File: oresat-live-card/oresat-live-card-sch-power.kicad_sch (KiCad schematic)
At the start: 116 parts, among them Q2 PMV45EN2R, Q3 DMP2240UDM-7, Q4 PMV45EN2R, Q5 DMP3050LVT-7, Q6 DMP3050LVT-7, U12 MIC842LYC5, U13 MIC842LYC5, U14 MAX4211, U15 LTC3624-5, U16 MAX7310, U21 TLV73311, U22 TS5A21366, U5 LTC3624-5

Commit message: Updated OPD / power page and synced with CFC processor, fixed layout issues.
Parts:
- added TP20, TP21, TP27, TP29: TEST-POINT, oresat-misc:TestPoint_Pad_D1.0mm, symbol oresat-misc:Test-Point-1mm-round
- D6, D7, D8, D9: value GREEN -> GRN
- Q3: value DMP2240UDM-7 -> DMP2240UDM; symbol oresat-transistors:DMP2240UDM-7 -> Transistor_FET:Q_Dual_PMOS_G1S2G2D2S1D1
- R50: value 0 -> 10k; DPN P0.0GCT-ND -> P10.0KHCT-ND; MPN ERJ-3GEY0R00V -> ERJ-3EKF1002V
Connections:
- net GND: now also TP20.1, TP21.1, TP27.1, TP29.1
- net at R51.2, TP57.1, U14.10 (CIN1+): now also R50.2; no longer R50.1
- net at U14.14 (IOUT): now also R50.1; no longer R50.2
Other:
- note added: "MAX7310 Address Selection R54, R55, R57 = 0x1B"
- note removed: "Address selection for Card (See MAX7310 datasheet)"
- note removed: "FIXME"
- note removed: "Install R54, R55, and R57 for Address 0x1B"
- note removed: "OreSat Power Enable (PEN)"
- moved on the sheet: C74, D6, R20, R22, R60, R92, R93, TP24, TP26, TP53, U22

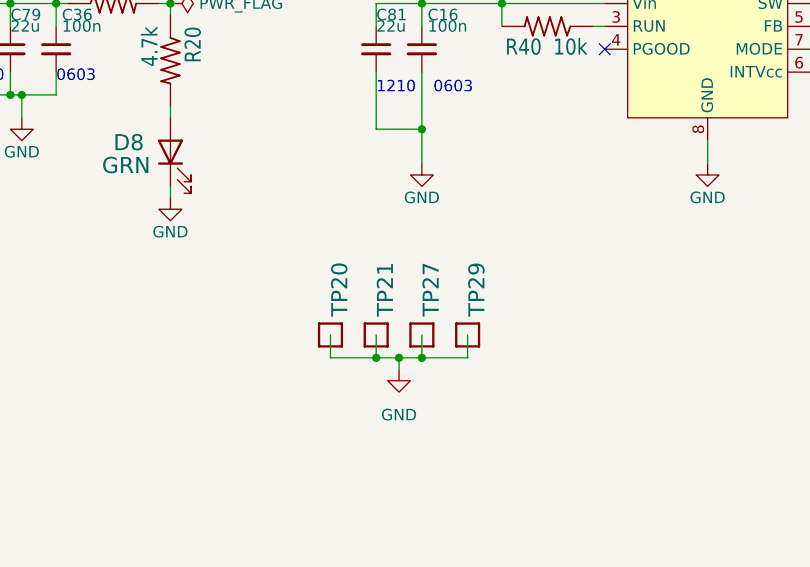
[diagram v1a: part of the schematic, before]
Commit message: Updated SIP A, B, and C. Lots of cleanup of crazy routing - this board is long in the tooth and has been rerouted several times, so there's a lot of crazy routing. Cleaning up a bit is really helping.
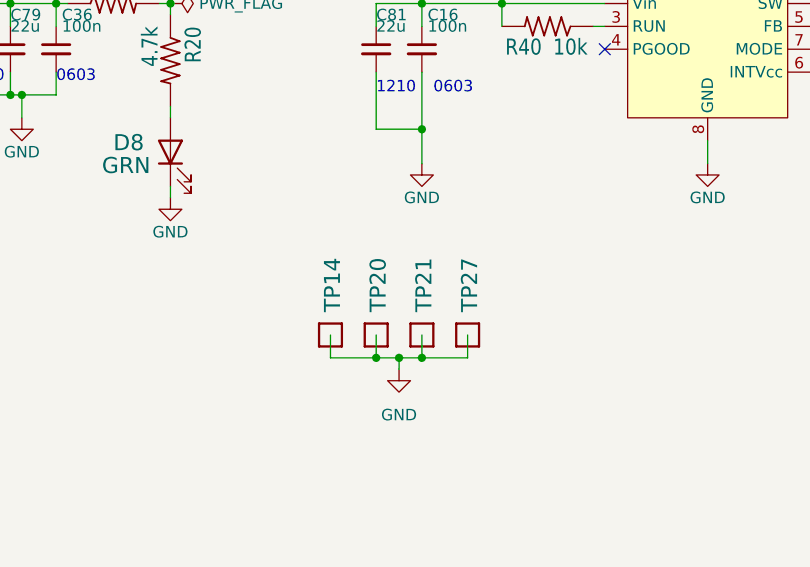
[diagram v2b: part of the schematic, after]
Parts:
- removed TP29: TEST-POINT, oresat-misc:TestPoint_Pad_D1.0mm, symbol oresat-misc:Test-Point-1mm-round
- added TP14: TEST-POINT, oresat-misc:TestPoint-0.75mm-th, symbol oresat-misc:Test-Point-1mm-round
- TP20, TP21, TP27: footprint oresat-misc:TestPoint_Pad_D1.0mm -> oresat-misc:TestPoint-0.75mm-th
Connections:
- net GND: now also TP14.1

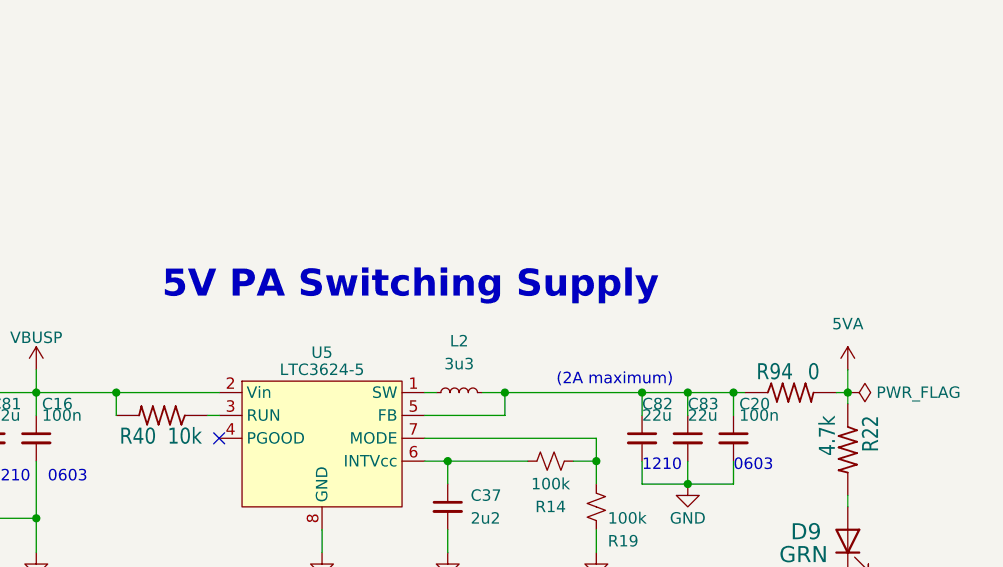
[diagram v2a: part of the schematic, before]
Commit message: Clean up DRC errors, thermistor routing clenup
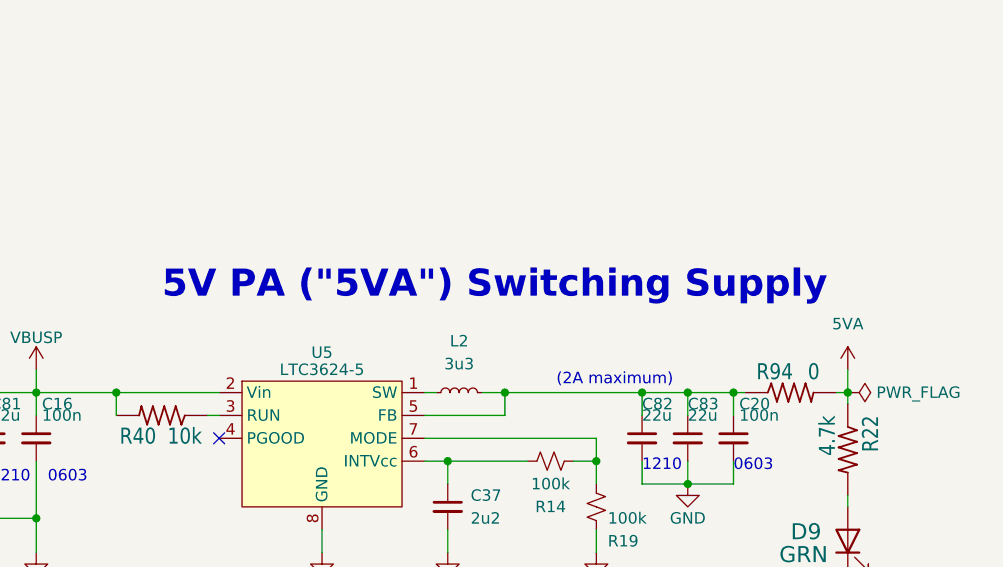
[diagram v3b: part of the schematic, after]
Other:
- note added: "5V PA ("5VA") Switching Supply"
- note removed: "5V PA Switching Supply"
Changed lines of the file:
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@@
 		)
 	)
-	(text "5V PA Switching Supply"
+	(text "5V PA (\"5VA\") Switching Supply"
 		(exclude_from_sim no)
 		(at 326.39 208.28 0)

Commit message: added Olivers BOM and footprint changes, cleaned up pcb
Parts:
- C16, C20, C3, C33, C34, C36, C38, C39, C61, C62, C74, C77, C84, C85, R11, R12, R14, R19, R20, R22, R32, R33, R34, R35, R36, R37, R38, R39, R40, R41, R43, R44, R45, R46, R47, R48, R49, R50, R51, R52, R54, R55, R57, R61, R64, R71, R72, R75, R92, R93, R95: footprint Resistor_SMD:R_0603_1608Metric -> oresat-passives:0603-C
- C17, C37: footprint Capacitor_SMD:C_0603_1608Metric -> oresat-passives:0603-C; DPN 490-GRM188Z71C225ME43JCT-ND -> 445-5723-1-ND
- C32, C35, C44: footprint Resistor_SMD:R_0805_2012Metric -> oresat-passives:0805-C
- R59, R60, R94: footprint Resistor_SMD:R_0603_1608Metric -> oresat-passives:0603-C; MPN ERJ-3GEY0R00V -> ERJ-3GEY0R00V
- R63: footprint Resistor_SMD:R_1206_3216Metric -> oresat-passives:1206-C
- U12, U13: DIS (none) -> DigiKey; DPN (none) -> 576-2927-1-ND; MFR (none) -> Microchip Technology; MPN (none) -> MIC842LYC5-TR

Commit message: added 100p cap to U34 CTRL line, some BOM changes
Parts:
- C17, C37: DPN 445-5723-1-ND -> 490-GRM188Z71C225ME43JCT-ND
- R20, R22, R49, R51: DPN ERJ-3EKF4701V -> P4.70KHCT-ND
- R63: DPN 541-2740-1-ND -> P.10AUCT-ND; MFR Vishay Dale -> Panasonic; MPN RCWE1206R100FKEA -> ERJ-8BWFR100V
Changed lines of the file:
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@@
 			)
 		)
-		(property "DPN" "ERJ-3EKF4701V"
+		(property "DPN" "P4.70KHCT-ND"
 			(at 346.71 58.42 0)
 			(effects
@@
 			)
 		)
-		(property "DPN" "ERJ-3EKF4701V"
+		(property "DPN" "P4.70KHCT-ND"
 			(at 284.48 224.79 0)
 			(effects
@@
 			)
 		)
-		(property "DPN" "ERJ-3EKF4701V"
+		(property "DPN" "P4.70KHCT-ND"
 			(at 402.59 224.79 0)
 			(effects
@@
 			)
 		)
-		(property "DPN" "445-5723-1-ND "
+		(property "DPN" "490-GRM188Z71C225ME43JCT-ND"
 			(at 240.03 231.14 0)
 			(effects
@@
 			)
 		)
-		(property "DPN" "445-5723-1-ND "
+		(property "DPN" "490-GRM188Z71C225ME43JCT-ND"
 			(at 358.14 231.14 0)
 			(effects
@@
 			)
 		)
-		(property "Description" "RES 0.1 OHM 1% 1/2W 1206"
+		(property "Description" "RES 0.1 OHM 1% 1W 1206"
 			(at 293.37 40.64 0)
 			(effects
@@
 			)
 		)
-		(property "MPN" "RCWE1206R100FKEA"
+		(property "MPN" "ERJ-8BWFR100V"
 			(at 293.37 40.64 0)
 			(effects
@@
 			)
 		)
-		(property "DPN" "541-2740-1-ND "
+		(property "DPN" "P.10AUCT-ND"
 			(at 293.37 40.64 0)
 			(effects
@@
 			)
 		)
-		(property "MFR" "Vishay Dale "
+		(property "MFR" "Panasonic"
 			(at 293.37 40.64 0)
 			(effects
@@
 			)
 		)
-		(property "DPN" "ERJ-3EKF4701V"
+		(property "DPN" "P4.70KHCT-ND"
 			(at 205.74 86.36 0)
 			(effects

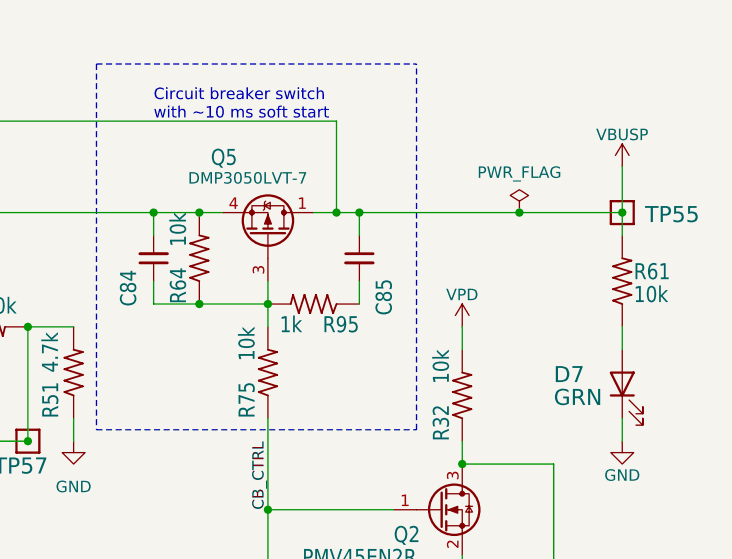
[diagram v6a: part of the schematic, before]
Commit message: OPD update
Updated component values
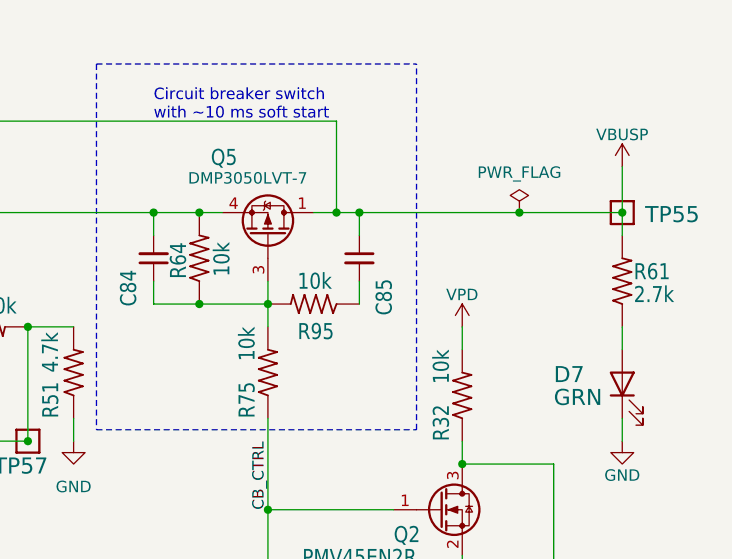
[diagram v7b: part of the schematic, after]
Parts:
- C84: value 1u -> 10n
- C85: value 1u -> 470n
- R61: value 10k -> 2.7k
- R95: value 1k -> 10k
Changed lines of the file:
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@@
 		(dnp no)
 		(property "Reference" "R95"
-			(at 378.46 52.07 0)
+			(at 375.666 52.832 0)
 			(show_name no)
 			(do_not_autoplace no)
@@
 			)
 		)
-		(property "Value" "1k"
-			(at 372.11 52.07 0)
+		(property "Value" "10k"
+			(at 375.412 47.244 0)
 			(show_name no)
 			(do_not_autoplace no)
@@
 		(dnp no)
 		(property "Reference" "R64"
-			(at 359.41 50.8 0)
+			(at 359.41 48.006 0)
 			(show_name no)
 			(do_not_autoplace no)
@@
 		)
 		(property "Value" "10k"
-			(at 359.41 44.45 0)
+			(at 364.236 47.752 0)
 			(show_name no)
 			(do_not_autoplace no)
@@
 			)
 		)
-		(property "Value" "10k"
+		(property "Value" "2.7k"
 			(at 408.94 50.8 90)
 			(show_name no)
@@
 			)
 		)
-		(property "Value" "1u"
+		(property "Value" "470n"
 			(at 378.46 45.72 0)
 			(hide yes)
@@
 			)
 		)
-		(property "Value" "1u"
+		(property "Value" "10n"
 			(at 355.6 45.72 0)
 			(hide yes)
